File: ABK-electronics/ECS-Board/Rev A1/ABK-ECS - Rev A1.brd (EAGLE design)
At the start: 80 x 80 mm, 139 parts, among them J1 1241050-5, J2 USB-B-S-RA, J3 22-27-2061-06, J4 22-05-7068-06, J5 22-05-7028-02, J6 22-05-7028-02, J7 22-05-7068-06, K3 G6K-2G-Y, SW1 B3FS-1015, SW2 B3FS-1015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

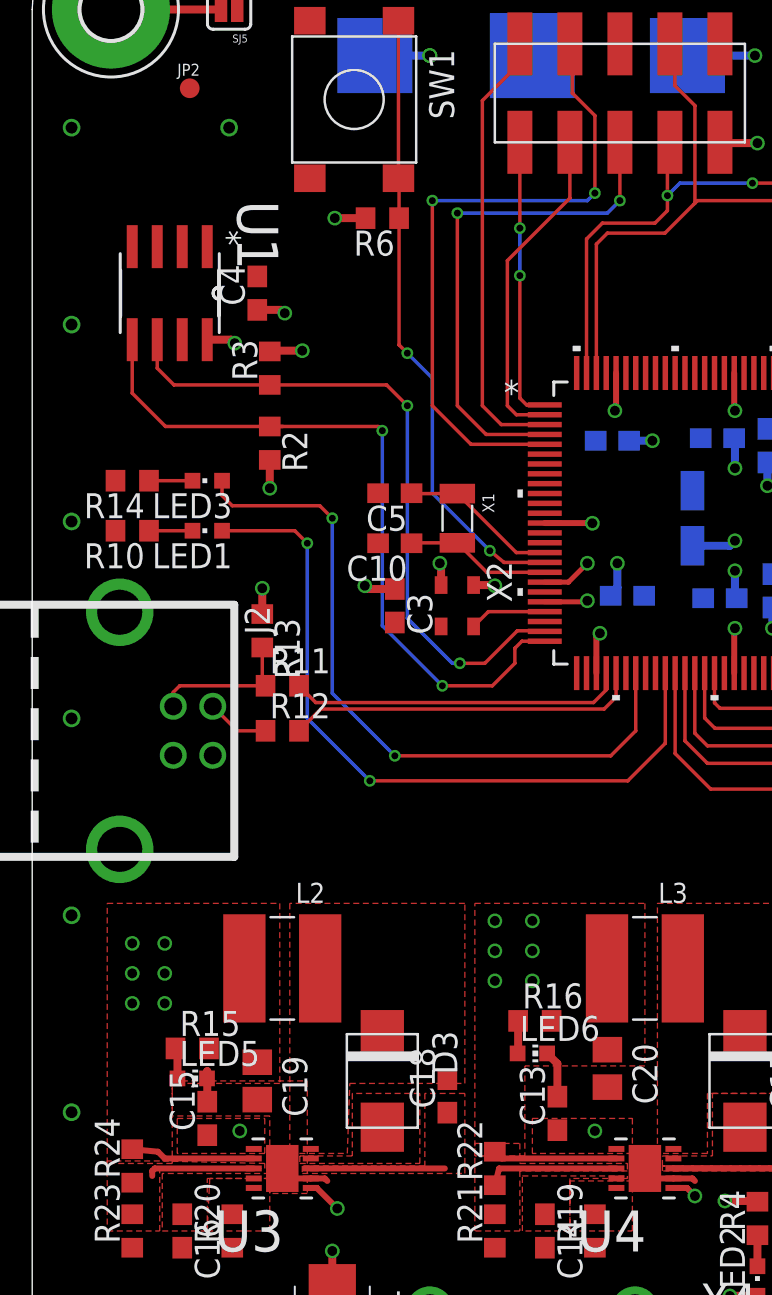
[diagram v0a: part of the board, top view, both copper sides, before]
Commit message: Rename guard ring to GND Put GND via under alim component Add a pull-down to WP on AT24
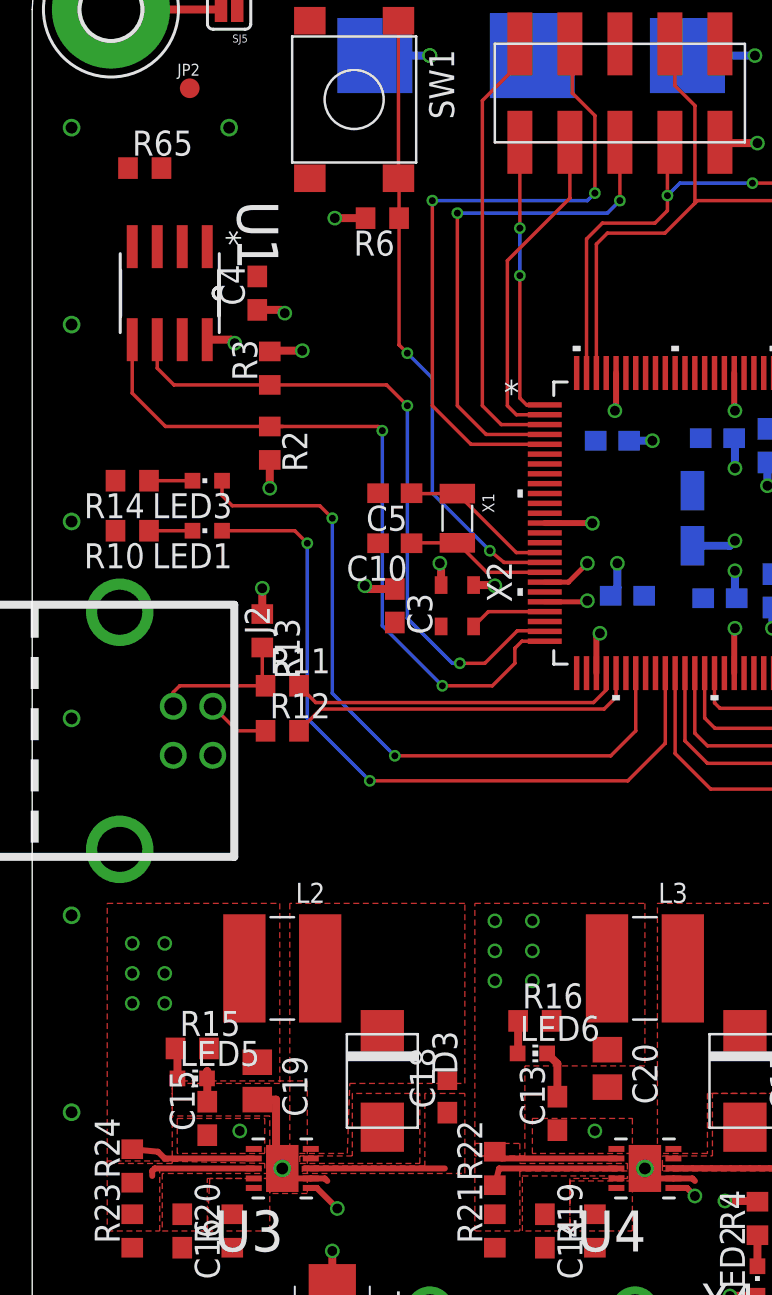
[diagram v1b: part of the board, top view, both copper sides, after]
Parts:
- added R65: 4K7, rcl:R0603
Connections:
- new net N$27: R65.1, U1.7
- net GND: now also R65.2; no longer U1.7
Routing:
- net GND: track 9.69 -> 14.5 mm, vias 0 -> 33
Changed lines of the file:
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@@
 <setting verticaltext="up"/>
 </settings>
-<grid distance="1" unitdist="mm" unit="mm" style="lines" multiple="10" display="yes" altdistance="25" altunitdist="mil" altunit="mil"/>
+<grid distance="25" unitdist="mil" unit="mil" style="lines" multiple="2" display="yes" altdistance="12.5" altunitdist="mil" altunit="mil"/>
 <layers>
 <layer number="1" name="Top" color="16" fill="1" visible="yes" active="yes"/>
@@
 <layer number="23" name="tOrigins" color="15" fill="1" visible="yes" active="yes"/>
 <layer number="24" name="bOrigins" color="15" fill="1" visible="yes" active="yes"/>
-<layer number="25" name="tNames" color="55" fill="1" visible="yes" active="yes"/>
+<layer number="25" name="tNames" color="55" fill="1" visible="no" active="yes"/>
 <layer number="26" name="bNames" color="54" fill="1" visible="no" active="yes"/>
-<layer number="27" name="tValues" color="53" fill="1" visible="yes" active="yes"/>
+<layer number="27" name="tValues" color="53" fill="1" visible="no" active="yes"/>
 <layer number="28" name="bValues" color="52" fill="1" visible="no" active="yes"/>
 <layer number="29" name="tStop" color="7" fill="3" visible="no" active="yes"/>
@@
 <element name="C21" library="rcl" package="C0603" value="0.1Uf" x="50.8" y="45.72" rot="R180"/>
 <element name="J2" library="con-multicomp" package="USB-B-S-RA" value="USB-B-S-RA" x="4.445" y="39.37" rot="R270"/>
+<element name="R65" library="rcl" package="R0603" value="4K7" x="5.715" y="67.945">
+<attribute name="MPN" value="MCMR06X4701FTL" x="5.715" y="67.945" size="1.778" layer="27" display="off"/>
+<attribute name="MF" value="" x="5.715" y="67.945" size="1.778" layer="27" display="off"/>
+<attribute name="OC_NEWARK" value="86T3649" x="5.715" y="67.945" size="1.778" layer="27" display="off"/>
+</element>
 </elements>
 <signals>
@@
 <vertex x="-10.795" y="87.63"/>
 </polygon>
-<contactref element="U1" pad="7"/>
 <polygon width="0.3048" layer="1" rank="6">
 <vertex x="7.112" y="19.939"/>
@@
 <contactref element="SJ5" pad="1"/>
 <contactref element="SJ4" pad="1"/>
+<via x="2" y="10" extent="1-16" drill="0.6"/>
+<via x="10" y="10" extent="1-16" drill="0.6"/>
+<via x="13" y="78" extent="1-16" drill="0.6"/>
+<via x="14" y="2" extent="1-16" drill="0.6"/>
+<via x="20" y="2" extent="1-16" drill="0.6"/>
+<via x="30" y="2" extent="1-16" drill="0.6"/>
+<via x="40" y="2" extent="1-16" drill="0.6"/>
+<via x="50" y="2" extent="1-16" drill="0.6"/>
+<via x="60" y="2" extent="1-16" drill="0.6"/>
+<via x="65" y="6" extent="1-16" drill="0.6"/>
+<via x="70" y="10" extent="1-16" drill="0.6"/>
+<via x="76" y="10" extent="1-16" drill="0.6"/>
+<via x="78" y="20" extent="1-16" drill="0.6"/>
+<via x="78" y="30" extent="1-16" drill="0.6"/>
+<via x="78" y="40" extent="1-16" drill="0.6"/>
+<via x="78" y="50" extent="1-16" drill="0.6"/>
+<via x="78" y="60" extent="1-16" drill="0.6"/>
+<via x="78" y="70" extent="1-16" drill="0.6"/>
+<via x="60" y="78" extent="1-16" drill="0.6"/>
+<via x="66" y="78" extent="1-16" drill="0.6"/>
+<via x="50" y="78" extent="1-16" drill="0.6"/>
+<via x="40" y="78" extent="1-16" drill="0.6"/>
+<via x="30" y="78" extent="1-16" drill="0.6"/>
+<via x="20" y="78" extent="1-16" drill="0.6"/>
+<via x="10" y="70" extent="1-16" drill="0.6"/>
+<via x="2" y="70" extent="1-16" drill="0.6"/>
+<via x="2" y="60" extent="1-16" drill="0.6"/>
+<via x="2" y="50" extent="1-16" drill="0.6"/>
+<via x="2" y="40" extent="1-16" drill="0.6"/>
+<via x="2" y="30" extent="1-16" drill="0.6"/>
+<via x="2" y="20" extent="1-16" drill="0.6"/>
+<via x="12.7" y="17.145" extent="1-16" drill="0.6"/>
+<via x="31.115" y="17.145" extent="1-16" drill="0.6"/>
+<wire x1="11.43" y1="20.64" x2="12.3825" y2="20.64" width="0.4064" layer="1"/>
+<wire x1="12.3825" y1="20.64" x2="12.3825" y2="17.145" width="0.4064" layer="1"/>
+<wire x1="12.7" y1="17.145" x2="12.3825" y2="17.145" width="0.4064" layer="1"/>
+<contactref element="R65" pad="2"/>
 </signal>
 <signal name="+3V3" class="2">
@@
 <wire x1="76" y1="76" x2="70.4119" y2="76" width="0.4064" layer="1"/>
 </signal>
-<signal name="N$27">
-<via x="14" y="2" extent="1-16" drill="0.6"/>
-</signal>
-<signal name="N$56">
-<via x="20" y="2" extent="1-16" drill="0.6"/>
-</signal>
-<signal name="N$57">
-<via x="30" y="2" extent="1-16" drill="0.6"/>
-</signal>
-<signal name="N$58">
-<via x="40" y="2" extent="1-16" drill="0.6"/>
-</signal>
-<signal name="N$59">
-<via x="50" y="2" extent="1-16" drill="0.6"/>
-</signal>
-<signal name="N$65">
-<via x="60" y="2" extent="1-16" drill="0.6"/>
-<via x="65" y="6" extent="1-16" drill="0.6"/>
-</signal>
-<signal name="N$66">
-<via x="76" y="10" extent="1-16" drill="0.6"/>
-</signal>
-<signal name="N$67">
-<via x="78" y="20" extent="1-16" drill="0.6"/>
-</signal>
-<signal name="N$68">
-<via x="78" y="30" extent="1-16" drill="0.6"/>
-</signal>
-<signal name="N$69">
-<via x="78" y="40" extent="1-16" drill="0.6"/>
-</signal>
-<signal name="N$70">
-<via x="78" y="50" extent="1-16" drill="0.6"/>
-</signal>
-<signal name="N$71">
-<via x="78" y="60" extent="1-16" drill="0.6"/>
-</signal>
-<signal name="N$72">
-<via x="78" y="70" extent="1-16" drill="0.6"/>
-</signal>
-<signal name="N$75">
-<via x="60" y="78" extent="1-16" drill="0.6"/>
-<via x="66" y="78" extent="1-16" drill="0.6"/>
-</signal>
-<signal name="N$76">
-<via x="50" y="78" extent="1-16" drill="0.6"/>
-</signal>
-<signal name="N$77">
-<via x="40" y="78" extent="1-16" drill="0.6"/>
-</signal>
-<signal name="N$78">
-<via x="30" y="78" extent="1-16" drill="0.6"/>
-</signal>
-<signal name="N$79">
-<via x="20" y="78" extent="1-16" drill="0.6"/>
-</signal>
-<signal name="N$80">
-<via x="2" y="70" extent="1-16" drill="0.6"/>
-</signal>
-<signal name="N$81">
-<via x="2" y="60" extent="1-16" drill="0.6"/>
-</signal>
-<signal name="N$83">
-<via x="2" y="50" extent="1-16" drill="0.6"/>
-</signal>
-<signal name="N$84">
-<via x="2" y="40" extent="1-16" drill="0.6"/>
-</signal>
-<signal name="N$85">
-<via x="2" y="30" extent="1-16" drill="0.6"/>
-</signal>
-<signal name="N$86">
-<via x="2" y="20" extent="1-16" drill="0.6"/>
-</signal>
-<signal name="N$87">
-<via x="2" y="10" extent="1-16" drill="0.6"/>
-</signal>
-<signal name="N$88">
-<via x="10" y="10" extent="1-16" drill="0.6"/>
-<via x="13" y="78" extent="1-16" drill="0.6"/>
-</signal>
-<signal name="N$89">
-<via x="70" y="10" extent="1-16" drill="0.6"/>
-</signal>
 <signal name="N$90">
 <via x="70" y="70" extent="1-16" drill="0.6"/>
 </signal>
-<signal name="N$91">
-<via x="10" y="70" extent="1-16" drill="0.6"/>
+<signal name="N$27">
+<contactref element="R65" pad="1"/>
+<contactref element="U1" pad="7"/>
+<wire x1="7.62" y1="59.2328" x2="4.865" y2="67.945" width="0" layer="19" extent="1-1"/>
 </signal>
 </signals>

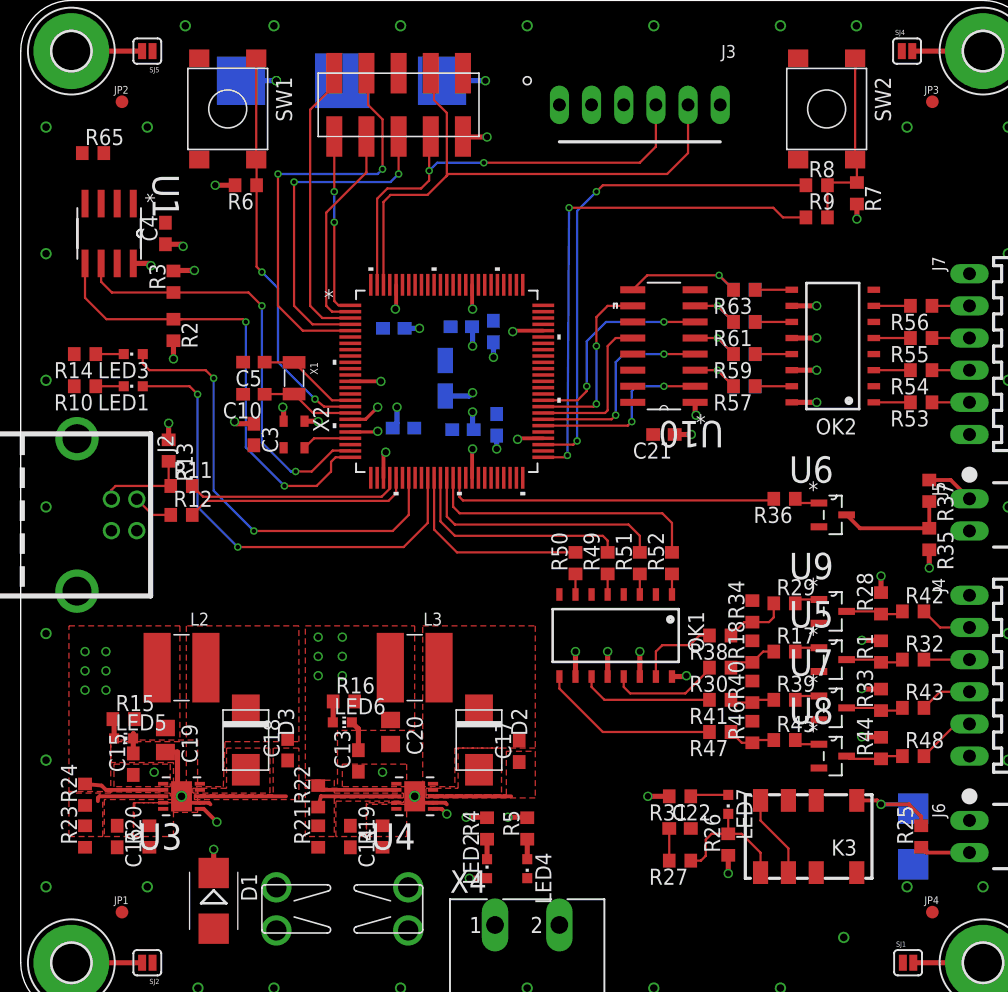
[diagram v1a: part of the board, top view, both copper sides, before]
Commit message: Add LEDs on input and output
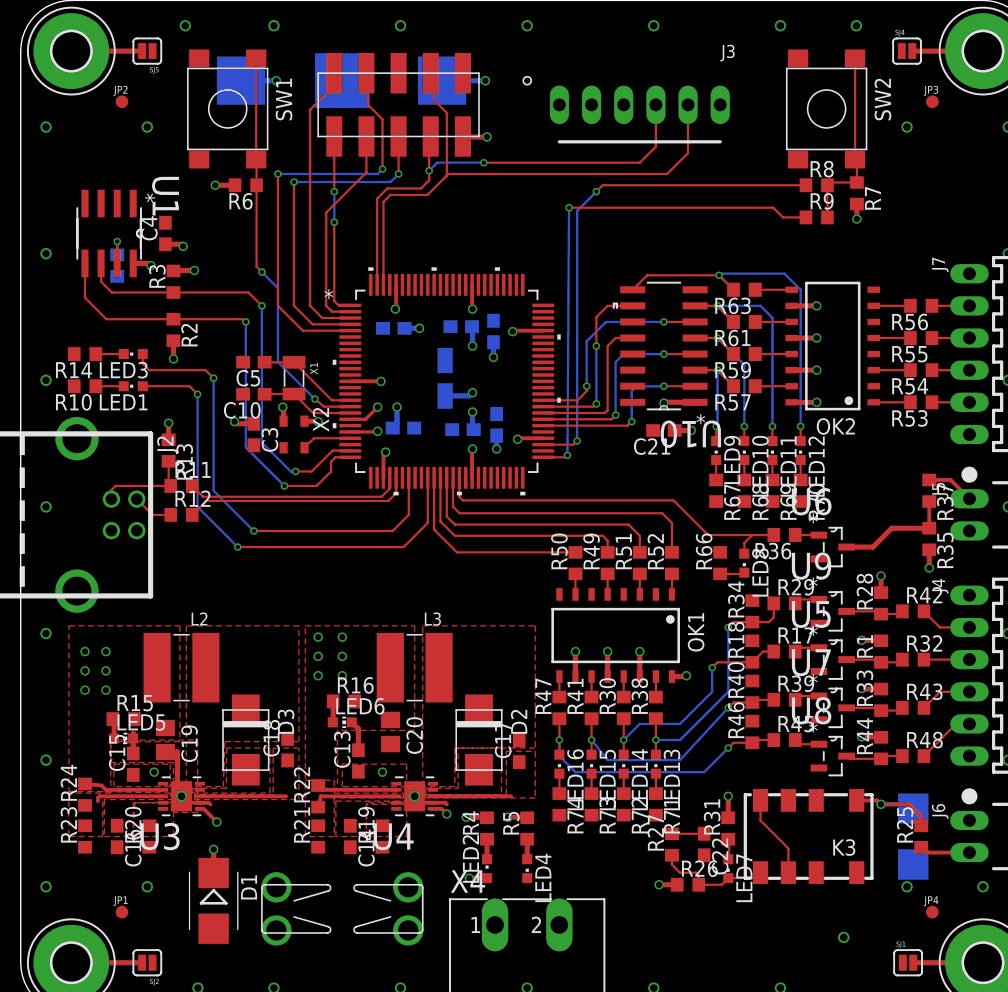
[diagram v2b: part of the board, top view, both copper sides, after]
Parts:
- added LED10, LED11, LED12, LED13, LED14, LED15, LED16, LED8, LED9: Blue, led:CHIPLED_0603
- added R66, R67, R68, R69, R70, R71, R72, R73, R74: 1K5, rcl:R0603
- LED7: value Blue -> Red
- moved R47 12.8 mm to (42.5, 24.1), turned to 90 degrees
- moved R41 10.2 mm to (45.1, 24.1), turned to 90 degrees
- moved R65 9.09 mm to (7.62, 59.1), flipped to the bottom, turned to 270 degrees
- moved R30 8.25 mm to (47.6, 24.1), turned to 90 degrees
- moved R38 7.65 mm to (50.2, 24.1), turned to 90 degrees
- moved LED7 5.08 mm to (55.9, 11.4)
- moved R31 4.58 mm to (55.9, 14.6), turned to 90 degrees
- moved R26 4.49 mm to (52.7, 10.2), turned to 0 degrees
- moved R36 2.86 mm to (60.3, 37.8)
- moved U6 2.54 mm to (64.1, 36.8)
- moved C22 2.29 mm to (54.0, 13.3), turned to 270 degrees
- moved R27 1.42 mm to (51.4, 13.3), turned to 90 degrees
- moved C21 0.32 mm to (50.8, 46.0)
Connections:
- new net N$56: LED8.C, R66.1
- new net N$57: LED9.C, R67.1
- new net N$58: LED10.C, R68.1
- new net N$59: LED11.C, R69.1
- new net N$65: LED12.C, R70.1
- new net N$66: LED13.C, R71.1
- new net N$67: LED14.C, R72.1
- new net N$68: LED15.C, R73.1
- new net N$69: LED16.C, R74.1
- net 230V-DETECTION: now also U2.43
- net DRIVE_STATUS_1: now also LED11.A
- net DRIVE_STATUS_2: now also LED12.A
- net EMERGENCY_STOP: now also LED9.A
- net GND: now also R66.2, R67.2, R68.2, R69.2, R70.2, R71.2, R72.2, R73.2, R74.2
- net LIMIT_SWITCH: now also LED10.A
- net MOTOR_CONTROL_MCU: now also LED8.A
- net N$20: now also LED13.A
- net N$25: now also LED14.A
- net N$34: now also LED15.A
- net N$37: now also LED16.A
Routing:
- net DRIVE_STATUS_2: track 10.5 -> 29.5 mm, vias 1 -> 2
- net N$37: track 3.82 -> 22.6 mm, vias 0 -> 2
- net N$34: track 3.56 -> 20.1 mm, vias 0 -> 2
- net N$20: track 5.08 -> 20.2 mm, vias 0 -> 2
- net N$25: track 3.91 -> 18.8 mm, vias 0 -> 2
- net DRIVE_STATUS_1: track 5.36 -> 19.8 mm, vias 1 -> 2
- net N$39: track 14.2 -> 1.62 mm
- net N$38: track 10.6 -> 1.62 mm
- net LIMIT_SWITCH: track 5.36 -> 12.6 mm, vias 1 -> 2
- net N$30: track 8.72 -> 1.62 mm
- net EMERGENCY_STOP: track 5.36 -> 11.0 mm, vias 1 -> 2
- net N$21: track 6.73 -> 1.62 mm
- net MOTOR_CONTROL_MCU: track 26.5 -> 29.3 mm
- net N$27: track 0.00 -> 2.78 mm, vias 0 -> 1
- net N$56: track 0.00 -> 1.95 mm
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
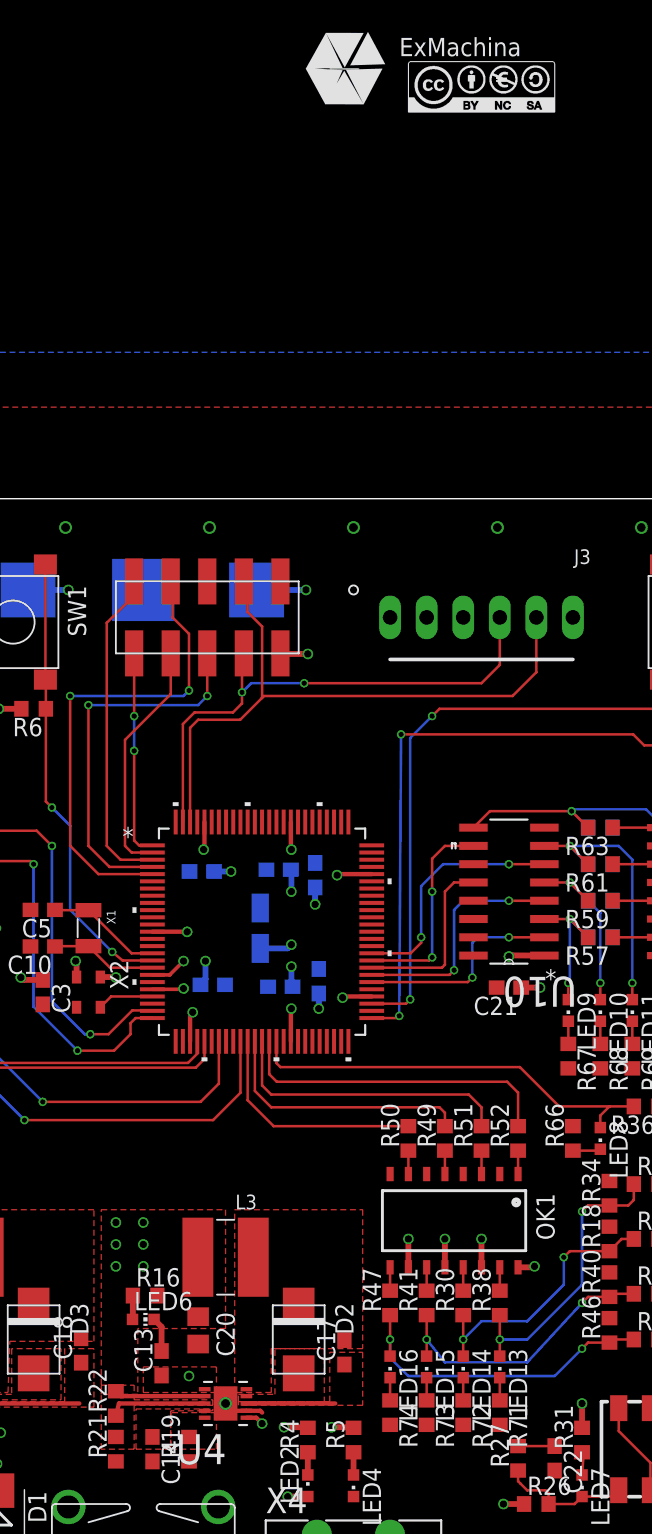
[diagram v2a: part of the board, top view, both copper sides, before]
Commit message: Place Logo and add name on the board
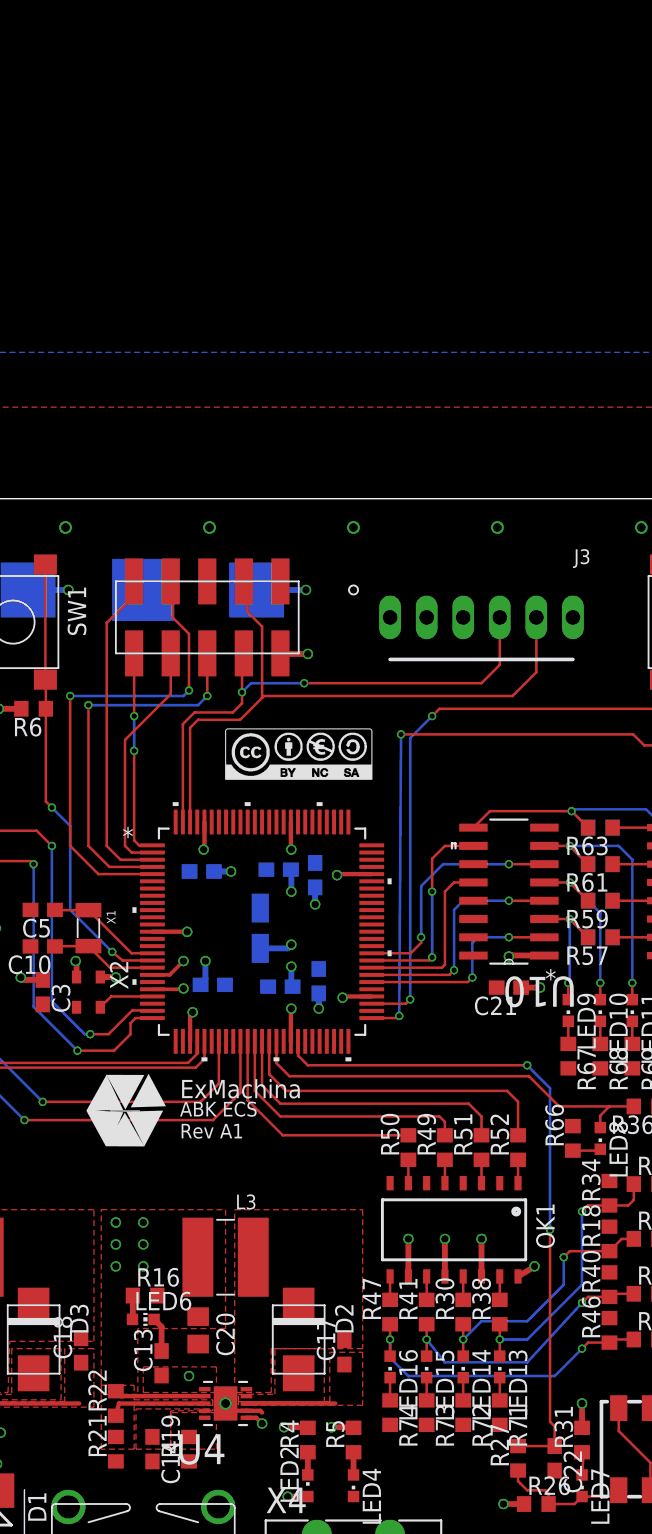
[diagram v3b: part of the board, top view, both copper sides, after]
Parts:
- moved T1 74.0 mm to (24.1, 37.5)
- moved CC1 48.1 mm to (36.2, 62.2)
- moved R49 0.64 mm to (46.4, 34.9)
- moved R50 0.64 mm to (43.8, 34.9)
- moved R51 0.64 mm to (48.9, 34.9)
- moved R52 0.64 mm to (51.4, 34.9)
- moved OK1 0.63 mm to (47.0, 29.2)
- moved R30 0.63 mm to (47.6, 23.5)
- moved R38 0.63 mm to (50.2, 23.5)
- moved R41 0.63 mm to (45.1, 23.5)
- moved R47 0.63 mm to (42.5, 23.5)
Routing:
- net 230V-DETECTION: track 2.54 -> 47.0 mm, vias 0 -> 2
- net +5V: track 24.4 -> 26.5 mm
- net N$37: track 22.6 -> 22.0 mm
- net N$34: track 20.1 -> 19.4 mm
- net N$25: track 18.8 -> 18.2 mm
- net N$20: track 20.2 -> 19.6 mm
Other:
- board text added: "ABK ECS Rev A1"
